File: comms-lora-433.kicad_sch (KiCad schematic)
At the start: 13 parts, among them J4 Conn_Coaxial_Small, U5 RFM69W

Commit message: Fixing lots of ERC errors
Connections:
- net SPI.MISO: now also R14.2; no longer R14.1, U5.14 (MOSI)
- net SPI.MOSI: now also R13.2; no longer R13.1, U5.13 (MISO)
- net SPI.SCK: now also R12.2; no longer R12.1, U5.12 (SCK)
- new net: R12.1, U5.12 (SCK)
- new net: R13.1, U5.13 (MISO)
- new net: R14.1, U5.14 (MOSI)
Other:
- moved on the sheet: C9, R12, R13, R14, R15

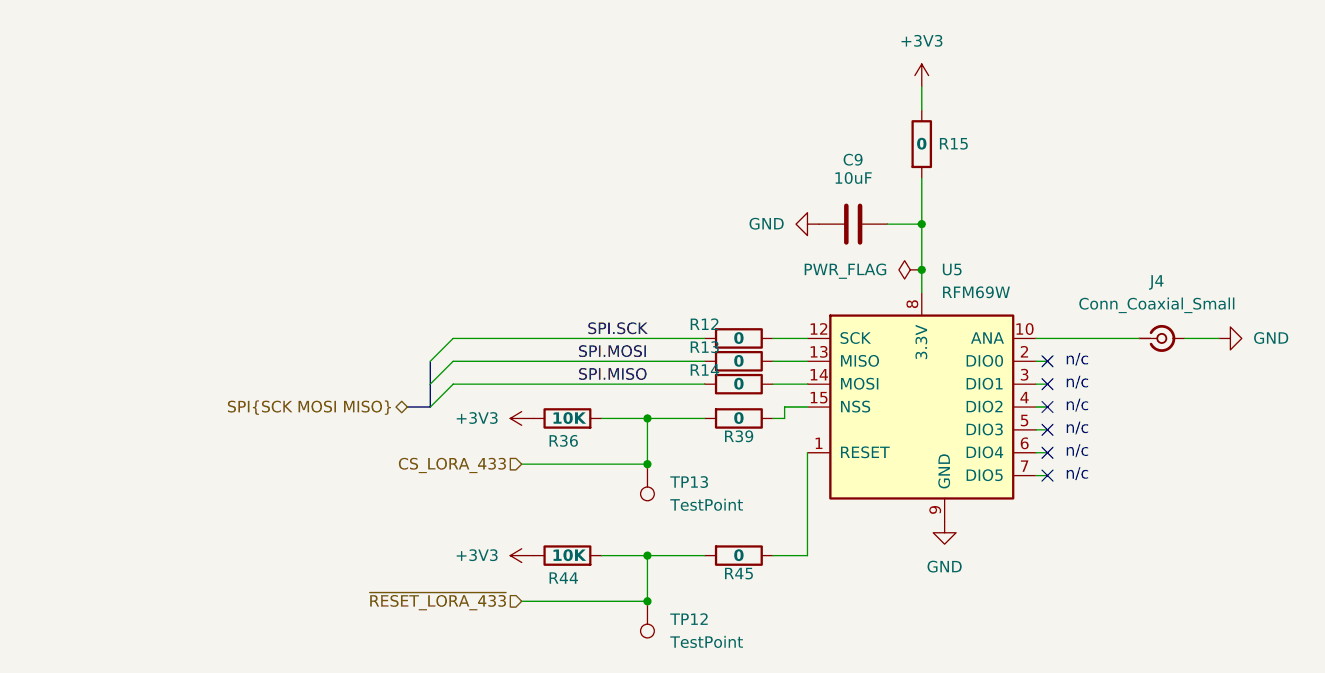
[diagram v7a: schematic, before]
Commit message: Redid board layout. Still have to add bypass caps
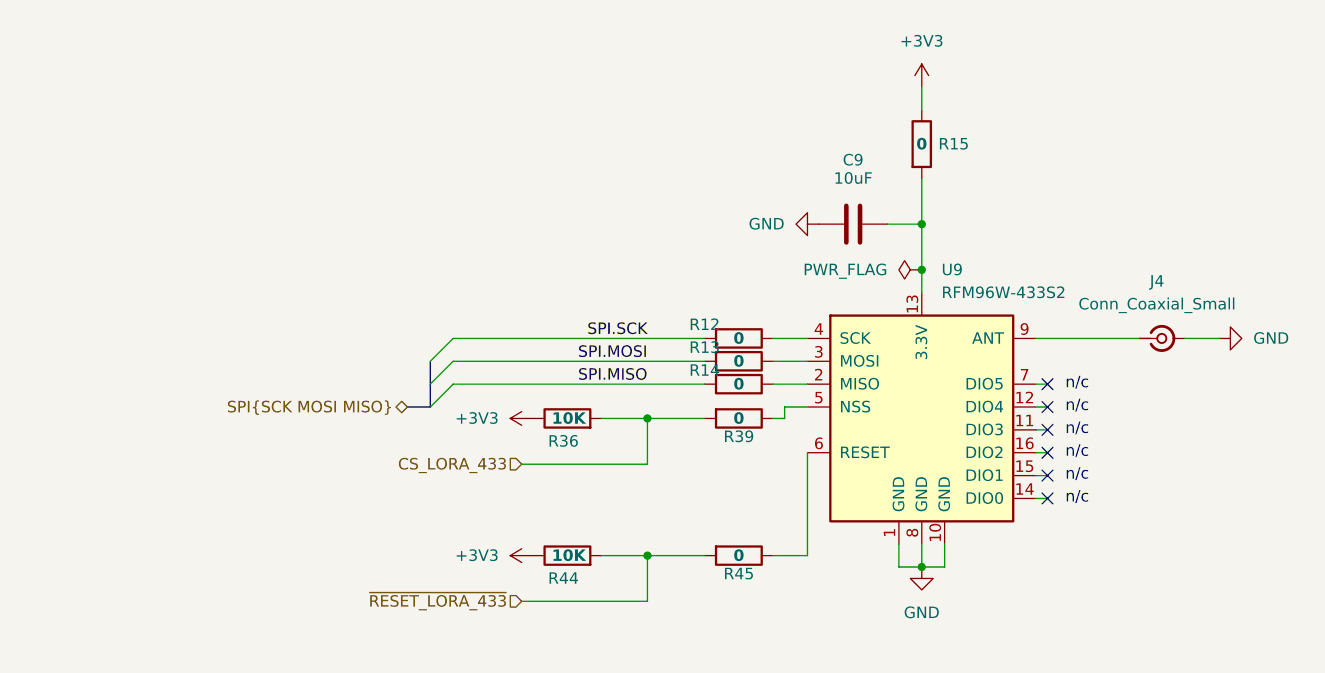
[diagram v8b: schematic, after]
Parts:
- removed TP12, TP13: TestPoint, TestPoint:TestPoint_Loop_D2.50mm_Drill1.0mm, symbol Connector:TestPoint
- removed U5: RFM69W, RF_Module:HOPERF_RFM69HW, symbol RF_Module:RFM69W
- added U9: RFM96W-433S2, RF_Module:HOPERF_RFM9XW_SMD, symbol RF_Module:RFM96W-433S2
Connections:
- net GND: now also U9.1 (GND), U9.10 (GND), U9.8 (GND)
- net at R45.1: now also U9.6 (RESET)
- net at J4.1 (In): now also U9.9 (ANT)
- net at R12.1: now also U9.4 (SCK)
- net at R13.1: now also U9.3 (MOSI)
- net at R14.1: now also U9.2 (MISO)
- net at R39.1: now also U9.5 (NSS)
- net at C9.2, R15.2: now also U9.13 (3.3V)
